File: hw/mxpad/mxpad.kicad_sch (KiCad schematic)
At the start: 20 parts, among them J1 COM-09032, J2 COM-09032, U1 WS2812B, U2 NodeMCU-12K, U3 MicroUSB

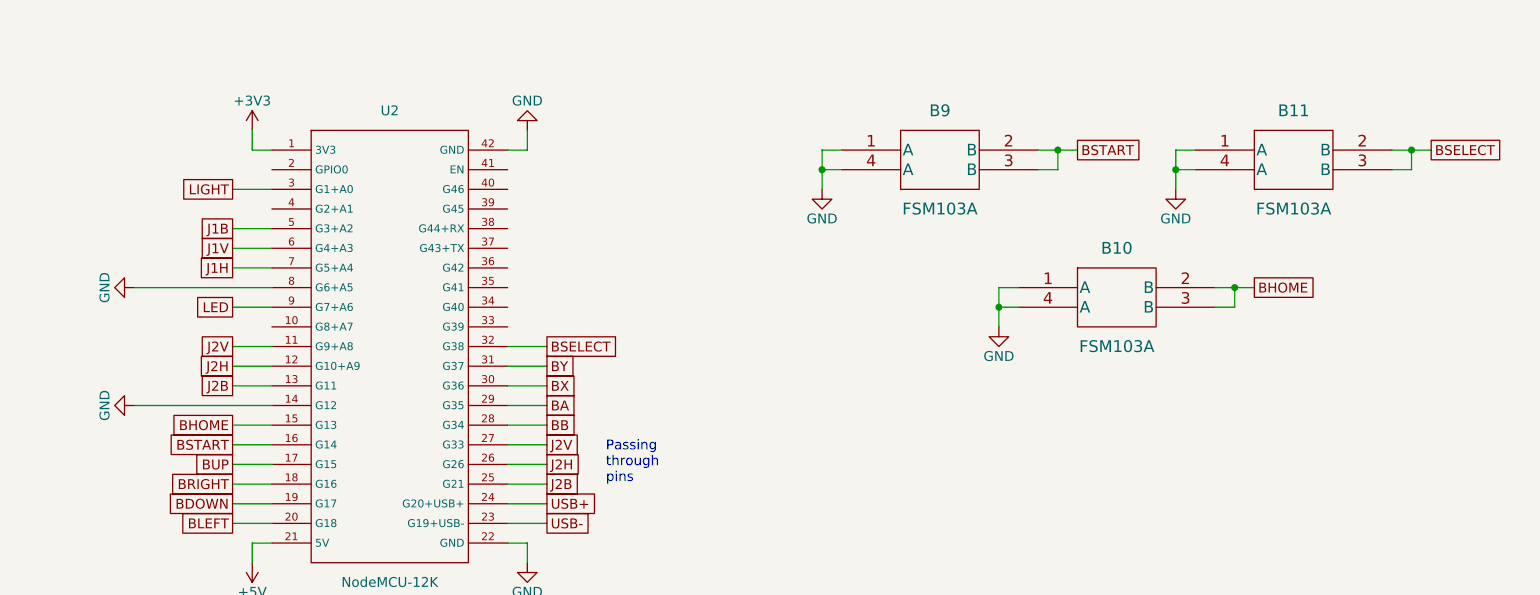
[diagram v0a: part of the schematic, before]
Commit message: Swap start / select on mxpad
Signed-off-by: Jan Hamal Dvořák <mordae@anilinux.org>
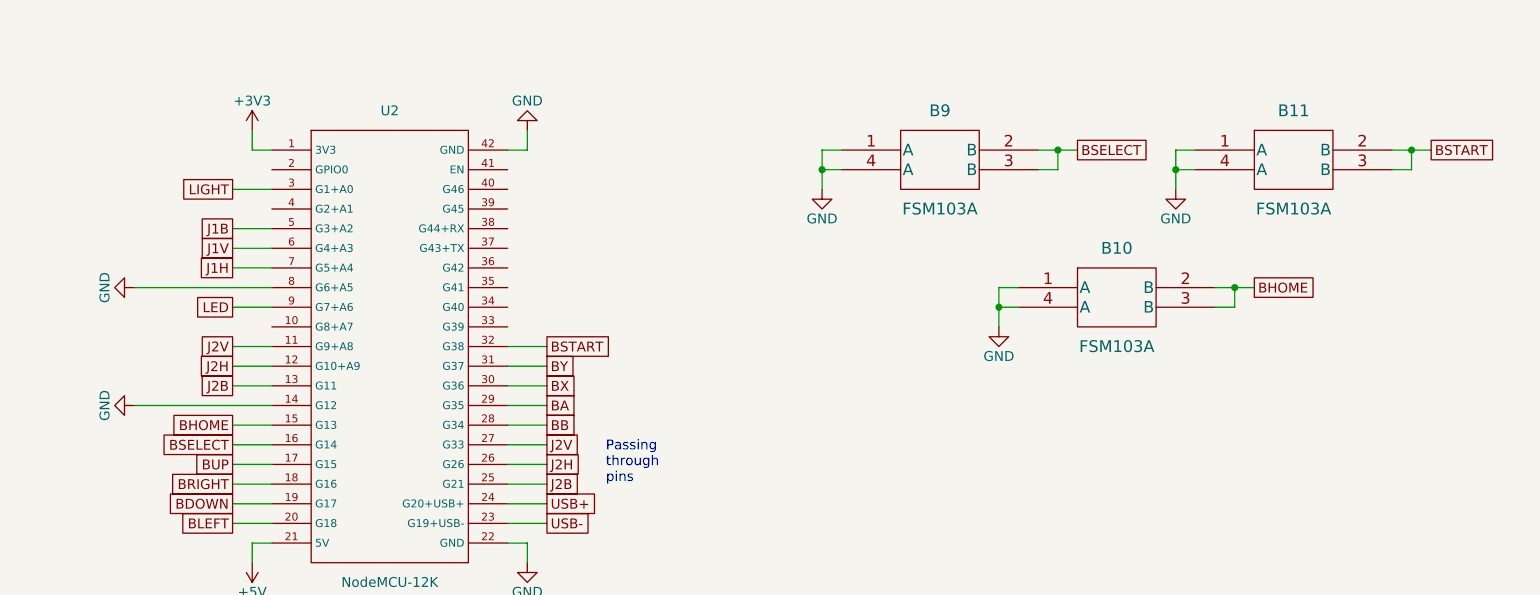
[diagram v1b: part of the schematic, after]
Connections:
- net BSELECT: now also B9.2 (B), B9.3 (B), U2.16 (G14); no longer B11.2 (B), B11.3 (B), U2.32 (G38)
- net BSTART: now also B11.2 (B), B11.3 (B), U2.32 (G38); no longer B9.2 (B), B9.3 (B), U2.16 (G14)
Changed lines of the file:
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@@
     )
   )
-  (global_label "BSELECT" (shape passive) (at 271.78 93.98 0) (fields_autoplaced)
+  (global_label "BSELECT" (shape passive) (at 226.06 93.98 0) (fields_autoplaced)
     (effects (font (size 1.27 1.27)) (justify left))
-    (property "Intersheet References" "${INTERSHEET_REFS}" (id 0) (at 282.2364 93.9006 0)
+    (property "Intersheet References" "${INTERSHEET_REFS}" (id 0) (at 236.5164 93.9006 0)
       (effects (font (size 1.27 1.27)) (justify left) hide)
     )
@@
     )
   )
-  (global_label "BSELECT" (shape passive) (at 157.48 119.38 0) (fields_autoplaced)
-    (effects (font (size 1.27 1.27)) (justify left))
-    (property "Intersheet References" "${INTERSHEET_REFS}" (id 0) (at 167.9364 119.3006 0)
-      (effects (font (size 1.27 1.27)) (justify left) hide)
+  (global_label "BSELECT" (shape passive) (at 116.84 132.08 180) (fields_autoplaced)
+    (effects (font (size 1.27 1.27)) (justify right))
+    (property "Intersheet References" "${INTERSHEET_REFS}" (id 0) (at 106.3836 132.1594 0)
+      (effects (font (size 1.27 1.27)) (justify right) hide)
     )
   )
@@
     )
   )
-  (global_label "BSTART" (shape passive) (at 226.06 93.98 0) (fields_autoplaced)
+  (global_label "BSTART" (shape passive) (at 271.78 93.98 0) (fields_autoplaced)
     (effects (font (size 1.27 1.27)) (justify left))
-    (property "Intersheet References" "${INTERSHEET_REFS}" (id 0) (at 235.2464 93.9006 0)
+    (property "Intersheet References" "${INTERSHEET_REFS}" (id 0) (at 280.9664 93.9006 0)
       (effects (font (size 1.27 1.27)) (justify left) hide)
     )
@@
     )
   )
-  (global_label "BSTART" (shape passive) (at 116.84 132.08 180) (fields_autoplaced)
-    (effects (font (size 1.27 1.27)) (justify right))
-    (property "Intersheet References" "${INTERSHEET_REFS}" (id 0) (at 107.6536 132.1594 0)
-      (effects (font (size 1.27 1.27)) (justify right) hide)
+  (global_label "BSTART" (shape passive) (at 157.48 119.38 0) (fields_autoplaced)
+    (effects (font (size 1.27 1.27)) (justify left))
+    (property "Intersheet References" "${INTERSHEET_REFS}" (id 0) (at 166.6664 119.3006 0)
+      (effects (font (size 1.27 1.27)) (justify left) hide)
     )
   )
